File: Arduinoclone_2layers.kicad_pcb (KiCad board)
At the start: 4 copper layers, 41.5 x 27.3 mm, 17 parts, among them J1 Digital pins, J2 Serial, J3 ICSP, J4 I2C, U1 24LC1025, U2 24LC1025, U3 DS13375+, U4 ATMEGA328-AU, Y1 32MHz, Y2 16MHz

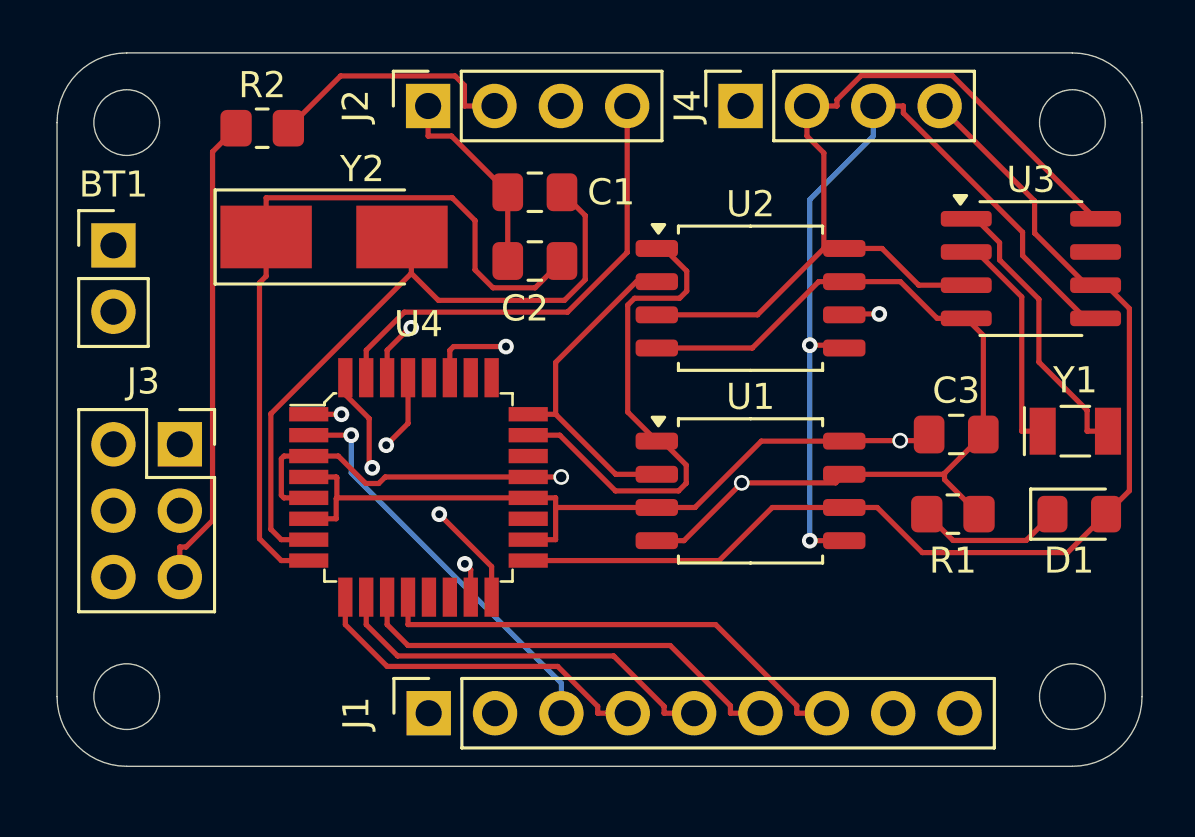
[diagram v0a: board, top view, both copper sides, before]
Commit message: Fully routed the board in 4 layers.
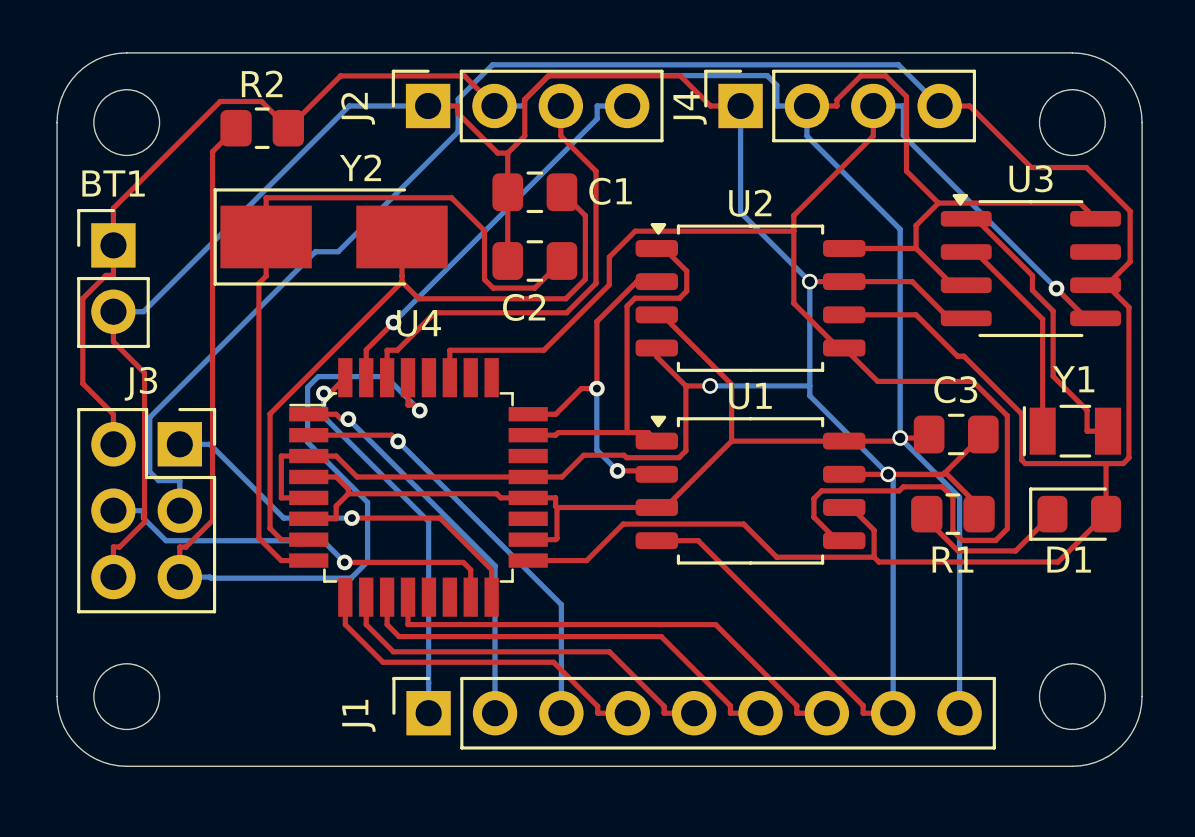
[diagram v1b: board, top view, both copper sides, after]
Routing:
- net /SCK: track 84.5 -> 104.2 mm, vias 1 -> 0
- net /SDA: track 47.8 -> 64.0 mm, vias 3 -> 1
- net /VCC: track 137.9 -> 126.6 mm
- net /RESET: track 31.1 -> 39.9 mm
- net /ADDS1: track 19.7 -> 14.7 mm
- net /RX: track 13.2 -> 17.5 mm, vias 1 -> 0
- net /TX: track 18.2 -> 15.2 mm, vias 0 -> 1
- net GNDPWR: track 128.1 -> 126.5 mm, vias 2 -> 3
- net /D4: track 15.6 -> 16.5 mm
- net /D2: track 14.2 -> 15.0 mm
- net /D3: track 16.0 -> 15.2 mm
- net /ADDS2: track 13.0 -> 13.6 mm, vias 0 -> 2
- net Net-(U3-X2): track 8.78 -> 8.27 mm
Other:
- copper layers 4 -> 2

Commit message: Created Copper fill area for 2 layer board
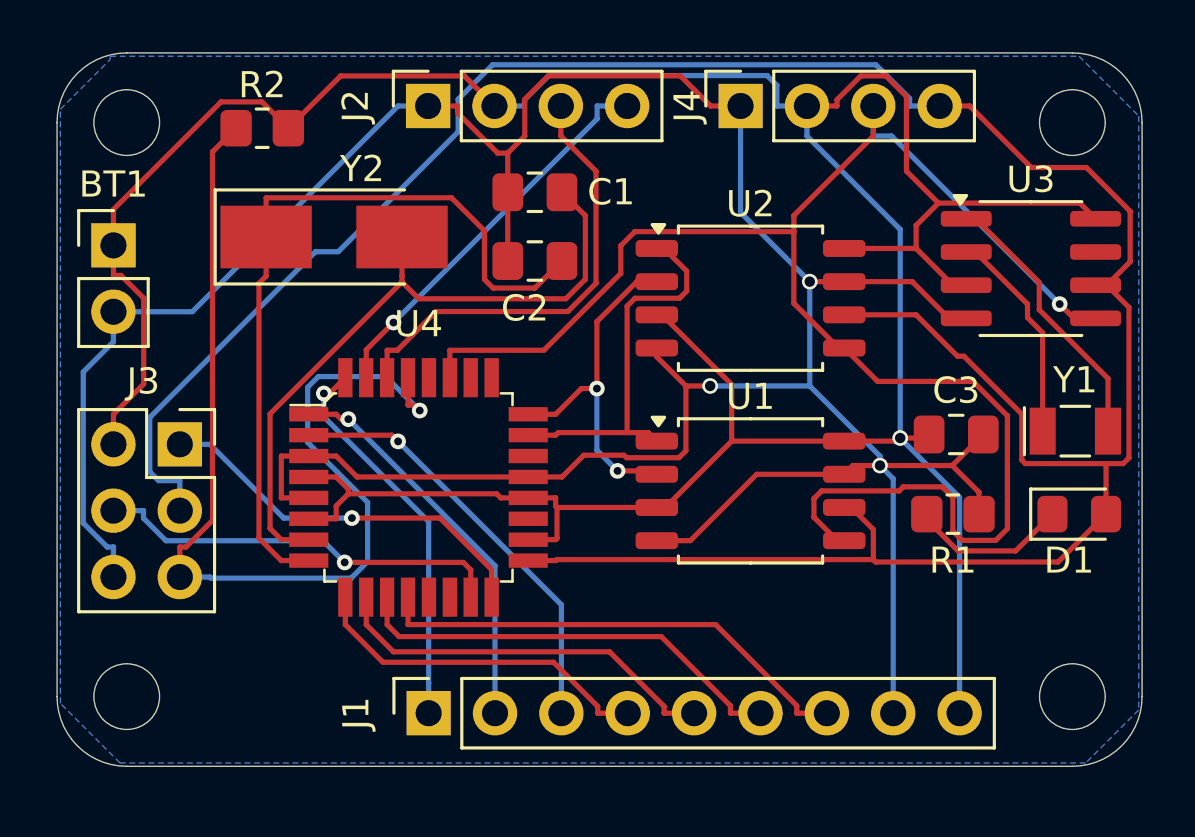
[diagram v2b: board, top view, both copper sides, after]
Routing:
- net GNDPWR: track 126.5 -> 122.9 mm
- net /SCK: track 104.2 -> 103.3 mm
- added copper zone on B.Cu, net GNDPWR

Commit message: Did the silkscreen.
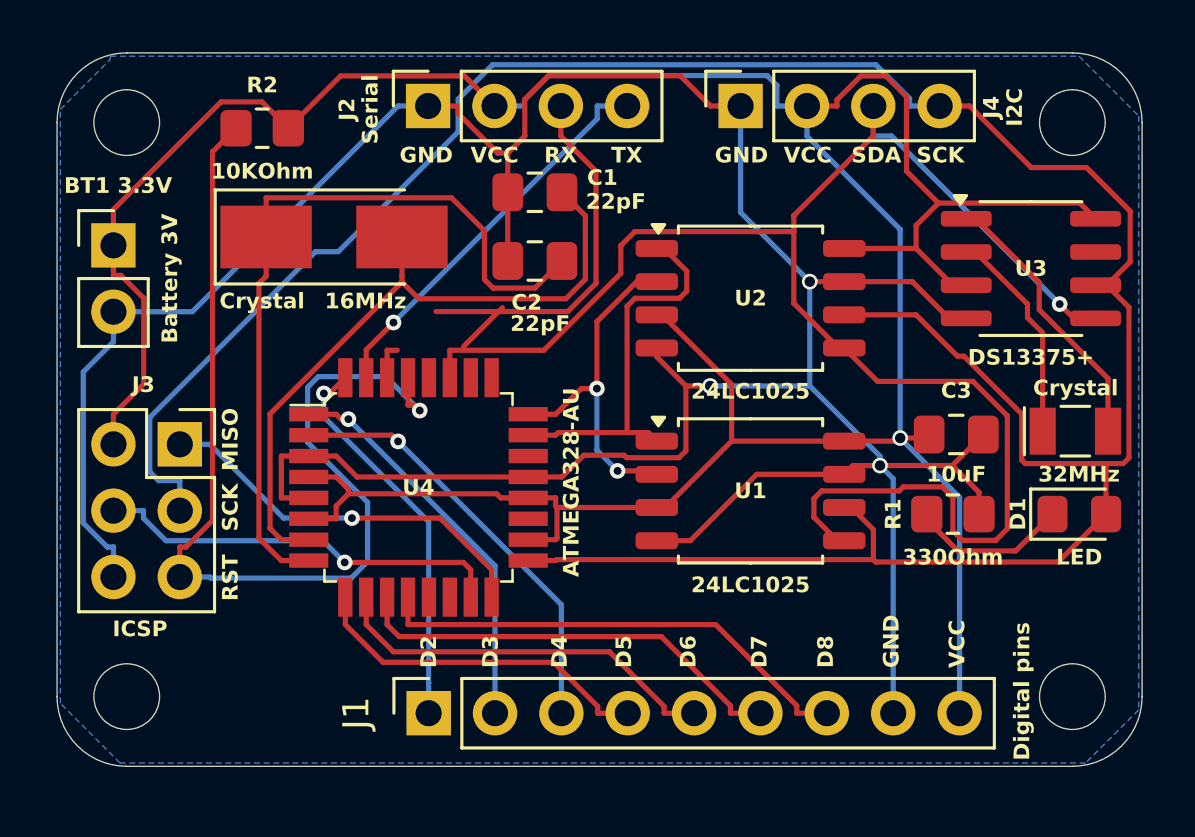
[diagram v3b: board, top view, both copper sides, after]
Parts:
- added REF**: OSHW-Logo2_9.8x8mm_SilkScreen, Symbol:OSHW-Logo2_9.8x8mm_SilkScreen, B.Cu at (159.9, 76.5)
- added REF**: KiCad-Logo2_6mm_SilkScreen, Symbol:KiCad-Logo2_6mm_SilkScreen, B.Cu at (176.4, 80.2)
- BT1 3.3V: renamed from BT1
- renumbered Y1 to Crystal
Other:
- board text added: "Arduino clone with: - 2Mbit EEPROM - Clock & calendar - I2C, SPI, GPIO"
- board text added: "D2"
- board text added: "D3"
- board text added: "D4"
- board text added: "D5"
- board text added: "D6"
- board text added: "D7"
- board text added: "D8"
- board text added: "GND"
- board text added: "MISO"
- board text added: "RST"
- board text added: "RX"
- board text added: "SCK"
- board text added: "SDA"
- board text added: "TX"
- board text added: "VCC"
